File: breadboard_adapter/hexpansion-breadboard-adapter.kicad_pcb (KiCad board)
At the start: 2 copper layers, 15.2 x 40.6 mm, 3 parts, among them J1 Conn_02x10_Counter_Clockwise, J2 Conn_01x10_Pin, J3 Conn_01x10_Pin

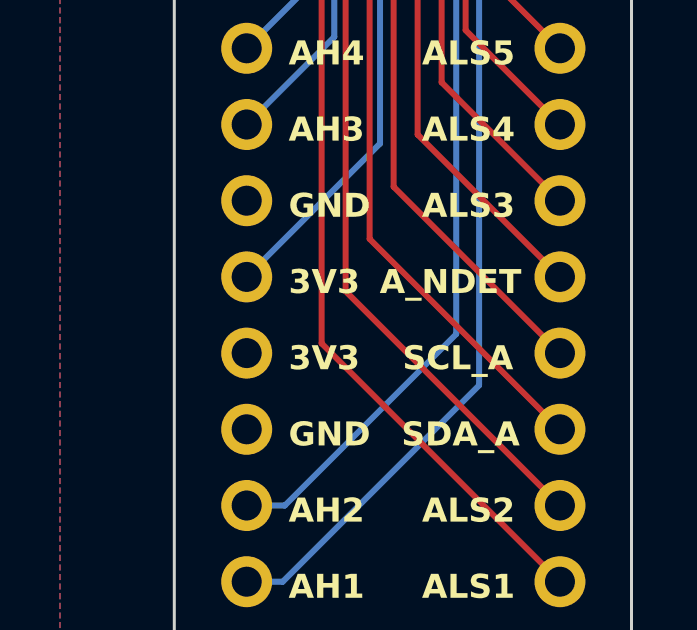
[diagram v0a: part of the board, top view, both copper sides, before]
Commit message: Update Breadboard Adapter.
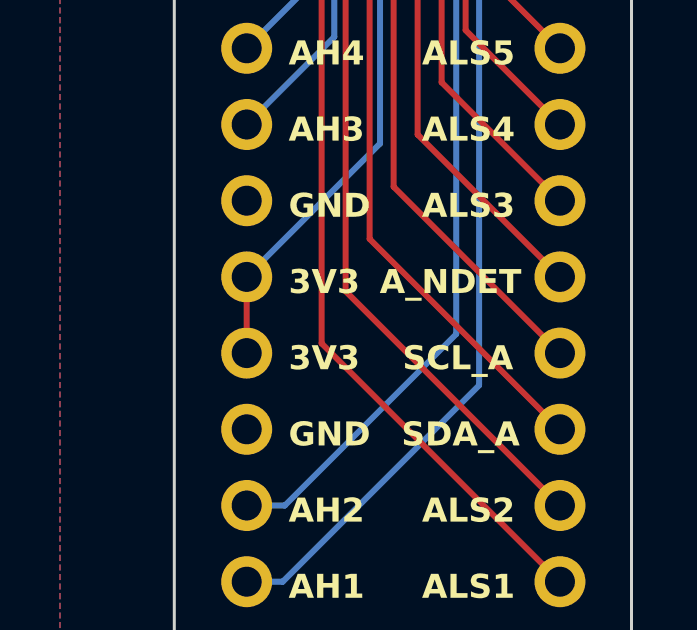
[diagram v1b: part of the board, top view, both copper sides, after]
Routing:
- net /PORTA_3V3: track 25.3 -> 27.9 mm
- added copper zone on B.Cu, net /GND
- added copper zone on F.Cu, net /GND
- removed copper zone on B.Cu, net (none)
- removed copper zone on F.Cu, net (none)
